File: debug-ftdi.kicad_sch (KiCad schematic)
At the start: 84 parts, among them J13 U_FL-R-SMT-1, J14 U_FL-R-SMT-1, J15 U_FL-R-SMT-1, J16 U_FL-R-SMT-1, J3 USB-C_GCT_USB4105-GF-A, J9 U_FL-R-SMT-1, Q20 BSS84AKW, U13 TXU0304BQAR, U16 TXS0102DQER, U32 TXS0102DQER, U5 NCP718BSN330T1G, U6 FT4232H_VQFN, U7 TXU0304BQAR, U8 TPD4E05U06QDQARQ1, U9 SN74HC595B, Y1 Resonator_12MHz_ABM8G

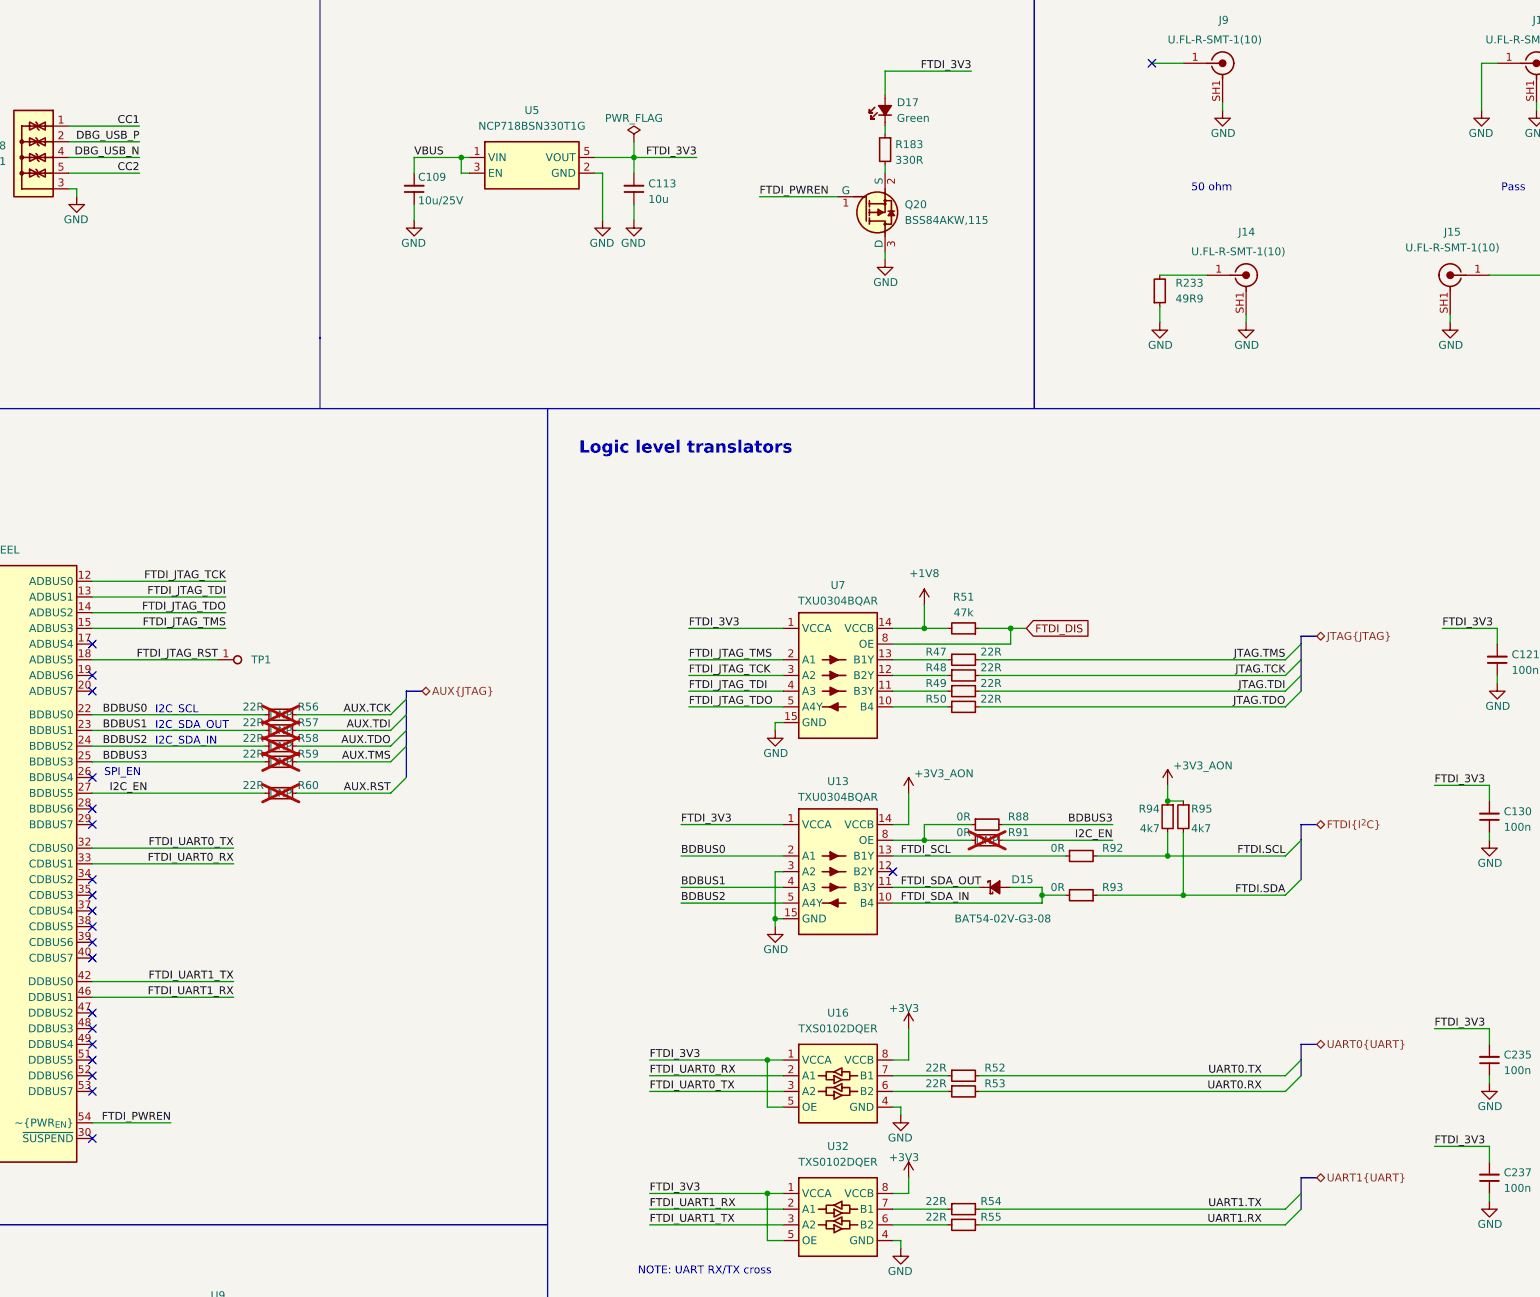
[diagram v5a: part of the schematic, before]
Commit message: [#68016] Improve bus entry marking
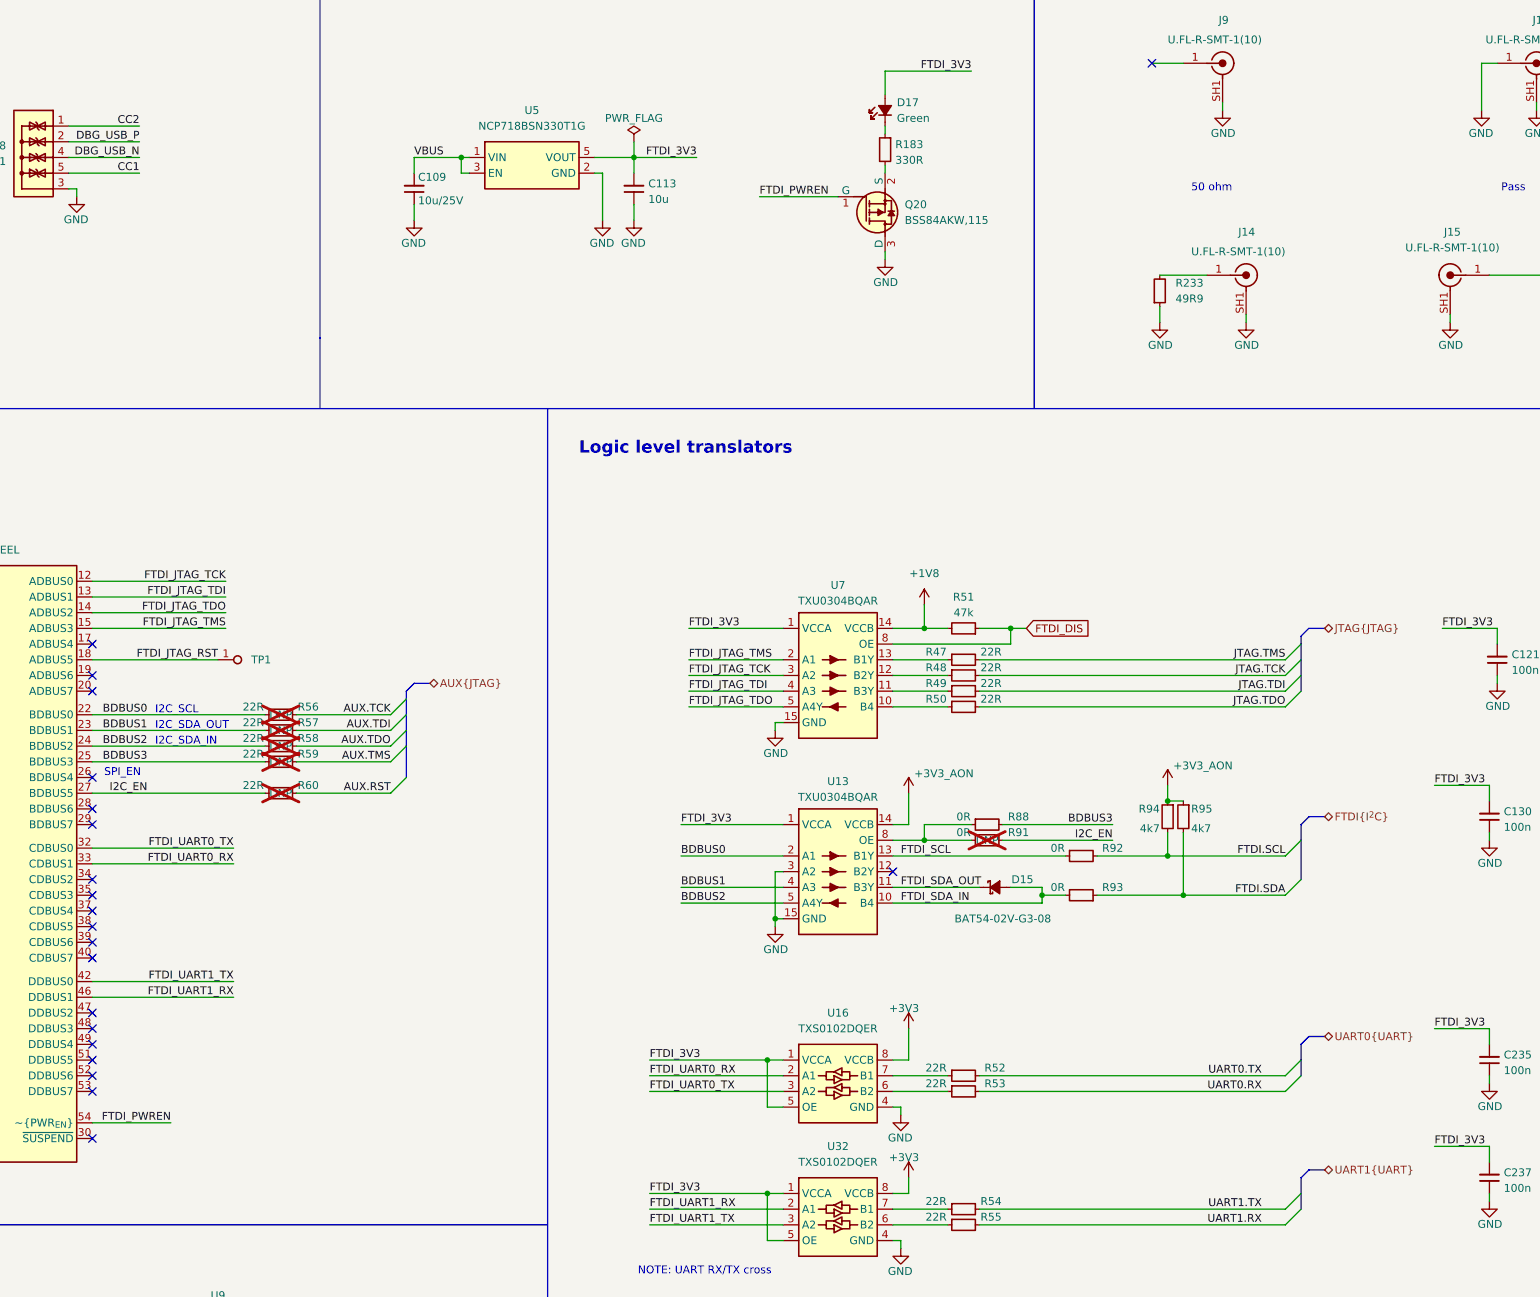
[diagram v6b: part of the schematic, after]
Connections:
- net CC1: now also U8.5, U8.6; no longer U8.1, U8.10
- net CC2: now also U8.1, U8.10; no longer U8.5, U8.6
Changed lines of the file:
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@@
     (stroke (width 0) (type default))
   )
+  (bus (pts (xy 341.63 134.62) (xy 342.9 133.35))
+    (stroke (width 0) (type default))
+  )
   (wire (pts (xy 384.81 200.66) (xy 384.81 198.12))
     (stroke (width 0) (type default))
@@
     (stroke (width 0) (type default))
   )
-  (bus (pts (xy 341.63 134.62) (xy 344.17 134.62))
+  (bus (pts (xy 342.9 133.35) (xy 345.44 133.35))
     (stroke (width 0) (type default))
   )
@@
     (stroke (width 0) (type default))
   )
+  (bus (pts (xy 196.85 143.51) (xy 198.12 142.24))
+    (stroke (width 0) (type default))
+  )
   (wire (pts (xy 241.3 165.1) (xy 257.81 165.1))
     (stroke (width 0) (type default))
@@
     (stroke (width 0) (type default))
   )
+  (bus (pts (xy 341.63 200.66) (xy 342.9 199.39))
+    (stroke (width 0) (type default))
+  )
   (wire (pts (xy 280.67 167.64) (xy 288.29 167.64))
     (stroke (width 0) (type default))
@@
     (stroke (width 0) (type default))
   )
+  (bus (pts (xy 341.63 222.25) (xy 342.9 220.98))
+    (stroke (width 0) (type default))
+  )
   (wire (pts (xy 49.53 127) (xy 49.53 129.54))
     (stroke (width 0) (type default))
@@
     (stroke (width 0) (type default))
   )
-  (bus (pts (xy 341.63 200.66) (xy 344.17 200.66))
+  (bus (pts (xy 342.9 199.39) (xy 345.44 199.39))
     (stroke (width 0) (type default))
   )
@@
     (stroke (width 0) (type default))
   )
+  (bus (pts (xy 341.63 165.1) (xy 342.9 163.83))
+    (stroke (width 0) (type default))
+  )
   (bus (pts (xy 196.85 147.32) (xy 196.85 149.86))
     (stroke (width 0) (type default))
@@
     (stroke (width 0) (type default))
   )
-  (bus (pts (xy 341.63 165.1) (xy 344.17 165.1))
+  (bus (pts (xy 342.9 163.83) (xy 345.44 163.83))
     (stroke (width 0) (type default))
   )
@@
     (stroke (width 0) (type default))
   )
-  (bus (pts (xy 341.63 222.25) (xy 344.17 222.25))
+  (bus (pts (xy 342.9 220.98) (xy 345.44 220.98))
     (stroke (width 0) (type default))
   )
@@
     (stroke (width 0) (type default))
   )
-  (bus (pts (xy 199.39 143.51) (xy 196.85 143.51))
+  (bus (pts (xy 200.66 142.24) (xy 198.12 142.24))
     (stroke (width 0) (type default))
   )
@@
     (effects (font (size 1.27 1.27)) (justify left bottom))
   )
-  (label "CC1" (at 153.67 52.07 180) (fields_autoplaced)
+  (label "CC1" (at 153.67 59.69 180) (fields_autoplaced)
     (effects (font (size 1.27 1.27)) (justify right bottom))
   )
@@
     (effects (font (size 1.27 1.27)) (justify right bottom))
   )
-  (label "CC2" (at 153.67 59.69 180) (fields_autoplaced)
+  (label "CC2" (at 153.67 52.07 180) (fields_autoplaced)
     (effects (font (size 1.27 1.27)) (justify right bottom))
   )
@@
     )
   )
-  (hierarchical_label "FTDI{I^{2}C}" (shape bidirectional) (at 344.17 165.1 0) (fields_autoplaced)
+  (hierarchical_label "FTDI{I^{2}C}" (shape bidirectional) (at 345.44 163.83 0) (fields_autoplaced)
     (effects (font (size 1.27 1.27)) (justify left))
   )
-  (hierarchical_label "UART1{UART}" (shape bidirectional) (at 344.17 222.25 0) (fields_autoplaced)
+  (hierarchical_label "UART1{UART}" (shape bidirectional) (at 345.44 220.98 0) (fields_autoplaced)
     (effects (font (size 1.27 1.27)) (justify left))
   )
-  (hierarchical_label "JTAG{JTAG}" (shape bidirectional) (at 344.17 134.62 0) (fields_autoplaced)
+  (hierarchical_label "JTAG{JTAG}" (shape bidirectional) (at 345.44 133.35 0) (fields_autoplaced)
     (effects (font (size 1.27 1.27)) (justify left))
   )
-  (hierarchical_label "UART0{UART}" (shape bidirectional) (at 344.17 200.66 0) (fields_autoplaced)
+  (hierarchical_label "UART0{UART}" (shape bidirectional) (at 345.44 199.39 0) (fields_autoplaced)
     (effects (font (size 1.27 1.27)) (justify left))
   )
-  (hierarchical_label "AUX{JTAG}" (shape bidirectional) (at 199.39 143.51 0) (fields_autoplaced)
+  (hierarchical_label "AUX{JTAG}" (shape bidirectional) (at 200.66 142.24 0) (fields_autoplaced)
     (effects (font (size 1.27 1.27)) (justify left))
   )

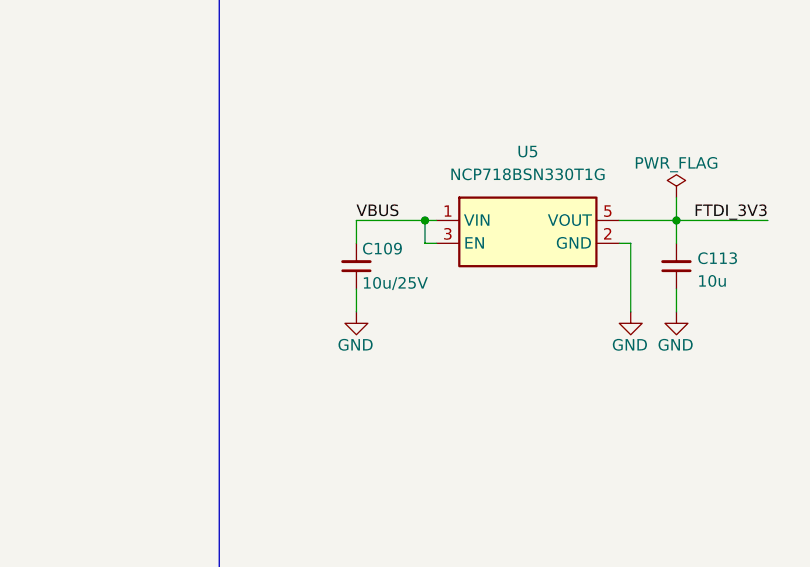
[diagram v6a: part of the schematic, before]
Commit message: [#68016] Solve ERC warrings and errors
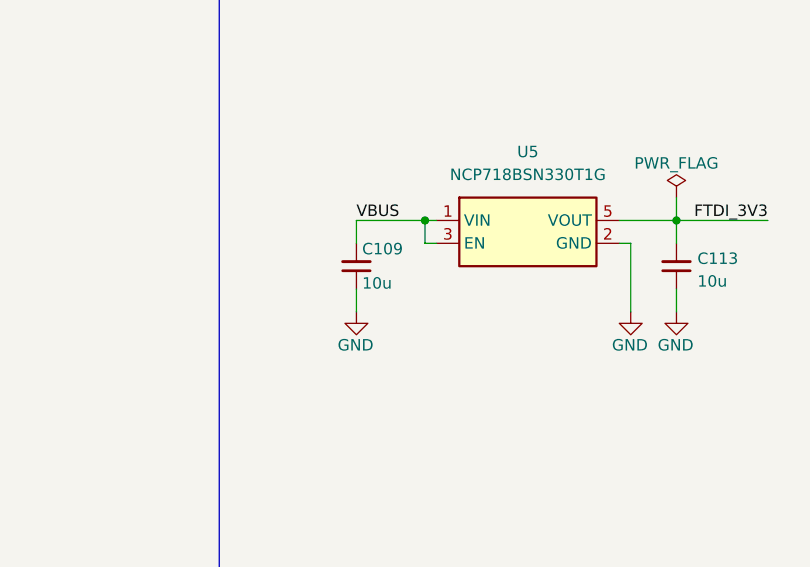
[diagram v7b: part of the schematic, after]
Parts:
- C109: Val 10u/25V -> 10u; Voltage (none) -> 25V
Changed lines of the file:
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@@
       (effects (font (size 1.27 1.27) (thickness 0.15)) (justify left bottom) hide)
     )
-    (property "Val" "10u/25V" (at 198.755 64.135 90)
+    (property "Val" "10u" (at 198.755 64.135 90)
       (effects (font (size 1.27 1.27) (thickness 0.15)) (justify right))
     )
@@
       (effects (font (size 1.27 1.27) (thickness 0.15)) (justify left bottom) hide)
     )
-    (property "Voltage" "" (at 226.06 44.45 0)
+    (property "Voltage" "25V" (at 226.06 44.45 0)
       (effects (font (size 1.27 1.27)) (justify left bottom) hide)
     )
@@
     )
   )
-  (symbol (lib_name "LED_G_0603_KP-1608CGCK_1") (lib_id "antmicroLEDIndicationDiscrete:LED_G_0603_KP-1608CGCK") (at 116.84 259.08 0) (unit 1)
+  (symbol (lib_id "antmicroLEDIndicationDiscrete:LED_G_0603_KP-1608CGCK") (at 116.84 259.08 0) (unit 1)
     (in_bom yes) (on_board yes) (dnp no)
     (property "Reference" "D11" (at 123.825 257.81 0)
@@
     )
   )
-  (symbol (lib_name "LED_G_0603_KP-1608CGCK_1") (lib_id "antmicroLEDIndicationDiscrete:LED_G_0603_KP-1608CGCK") (at 116.84 252.73 0) (unit 1)
+  (symbol (lib_id "antmicroLEDIndicationDiscrete:LED_G_0603_KP-1608CGCK") (at 116.84 252.73 0) (unit 1)
     (in_bom yes) (on_board yes) (dnp no)
     (property "Reference" "D10" (at 123.825 251.46 0)
@@
     )
   )
-  (symbol (lib_name "LED_G_0603_KP-1608CGCK_1") (lib_id "antmicroLEDIndicationDiscrete:LED_G_0603_KP-1608CGCK") (at 116.84 265.43 0) (unit 1)
+  (symbol (lib_id "antmicroLEDIndicationDiscrete:LED_G_0603_KP-1608CGCK") (at 116.84 265.43 0) (unit 1)
     (in_bom yes) (on_board yes) (dnp no)
     (property "Reference" "D12" (at 123.825 264.16 0)
@@
     )
   )
-  (symbol (lib_name "LED_G_0603_KP-1608CGCK_1") (lib_id "antmicroLEDIndicationDiscrete:LED_G_0603_KP-1608CGCK") (at 116.84 271.78 0) (unit 1)
+  (symbol (lib_id "antmicroLEDIndicationDiscrete:LED_G_0603_KP-1608CGCK") (at 116.84 271.78 0) (unit 1)
     (in_bom yes) (on_board yes) (dnp no)
     (property "Reference" "D13" (at 123.825 270.51 0)
